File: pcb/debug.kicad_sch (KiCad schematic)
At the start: 8 parts

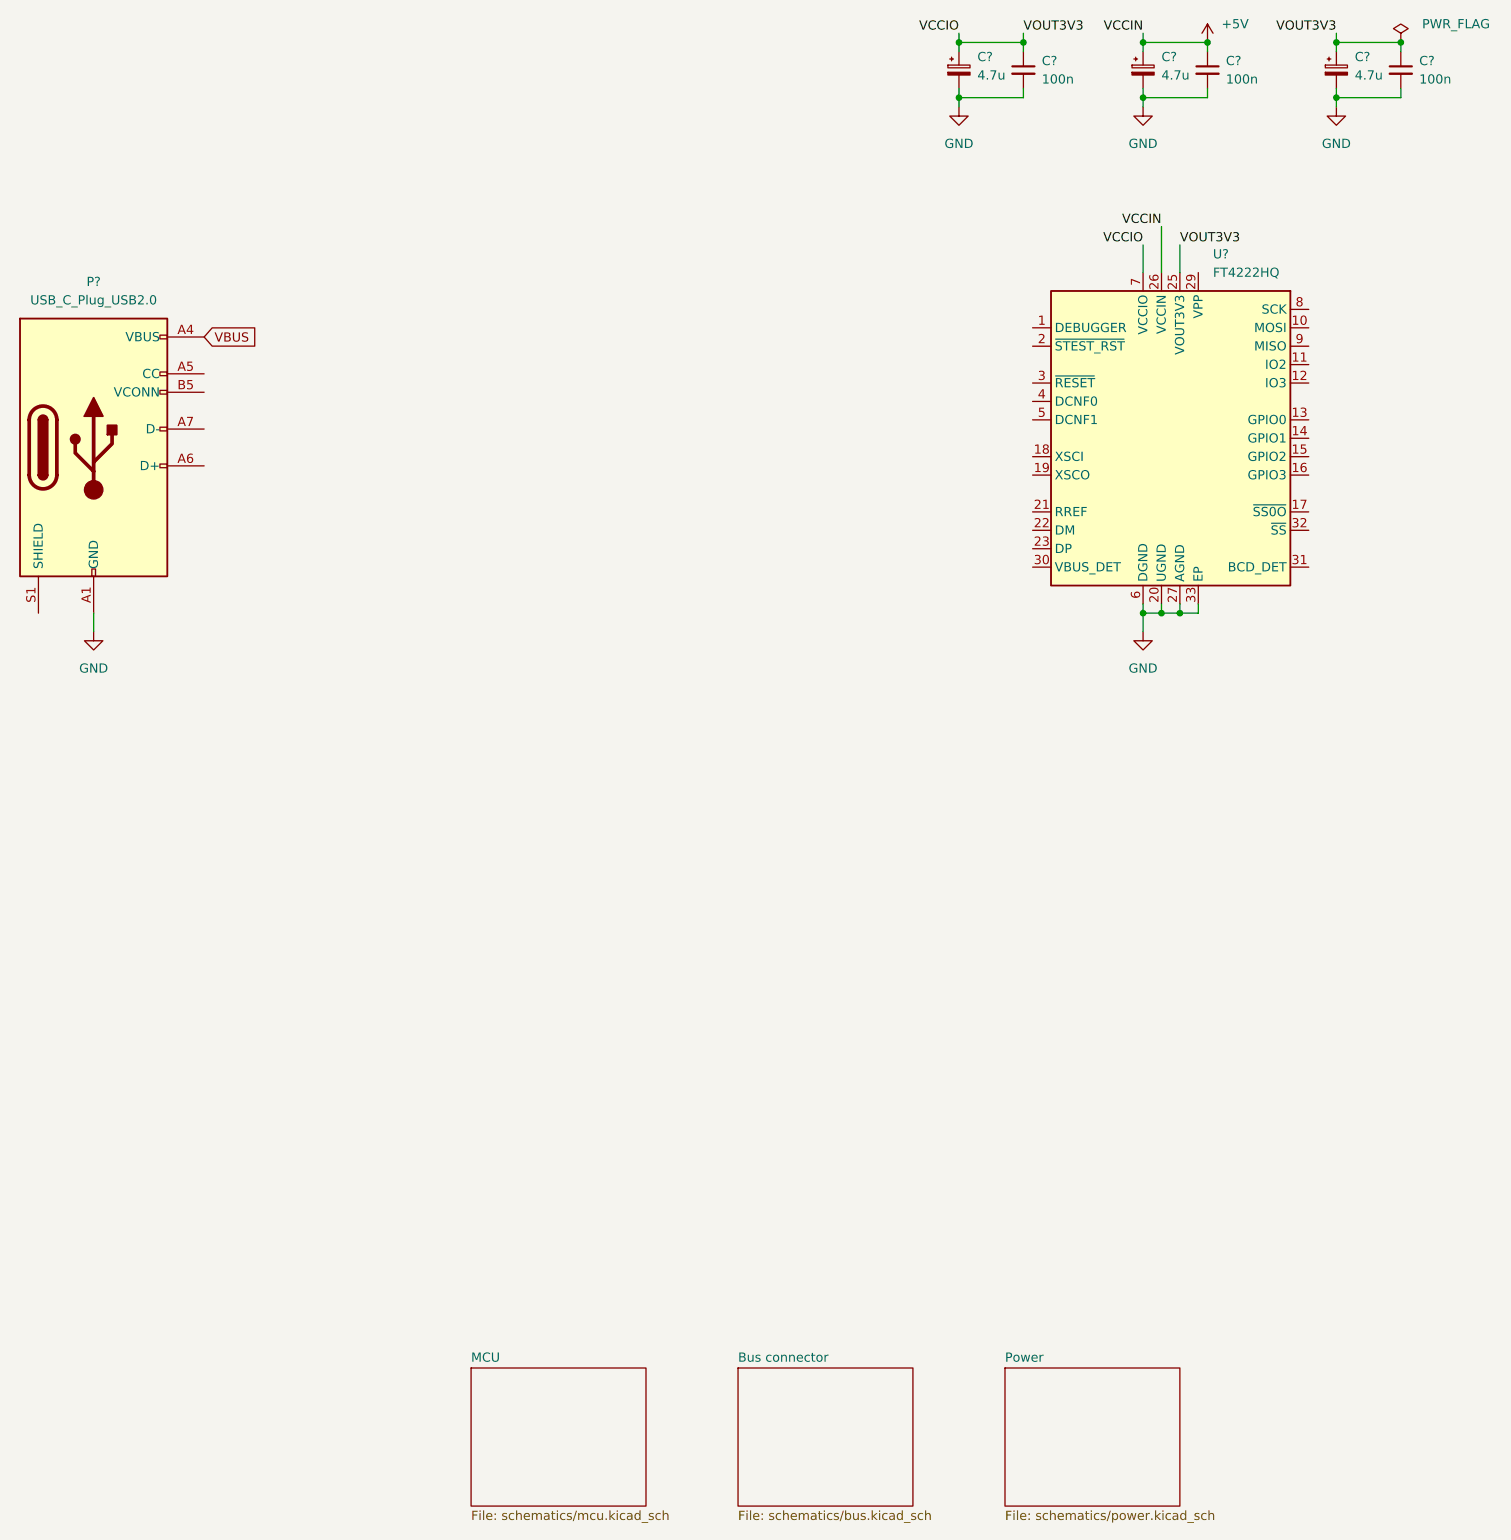
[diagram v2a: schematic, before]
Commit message: start choosing components, need to add overcurren t protection
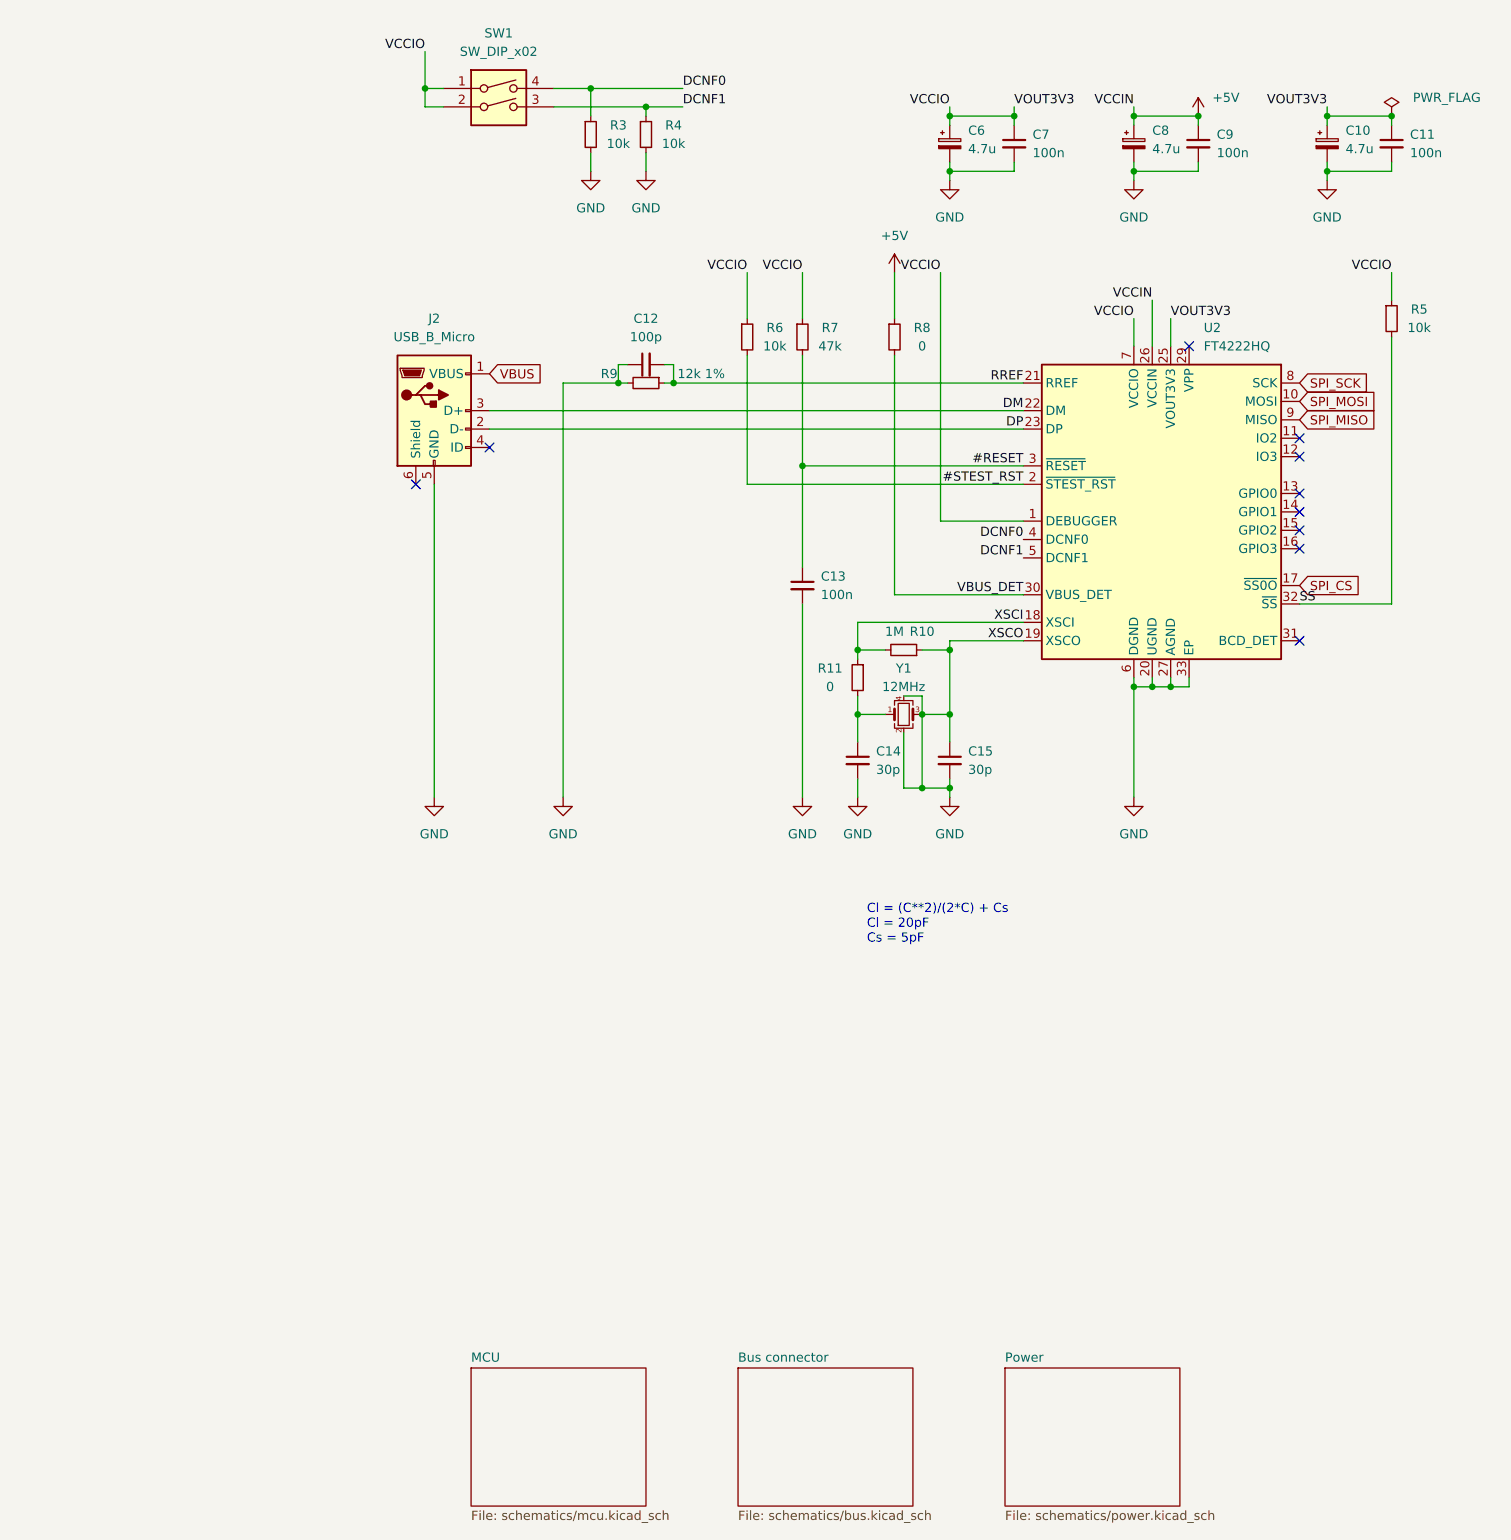
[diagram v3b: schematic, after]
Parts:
- removed P?: USB_C_Plug_USB2.0, symbol Connector:USB_C_Plug_USB2.0
- added C12: 100p, Capacitor_SMD:C_0603_1608Metric, symbol Device:C_Small
- added C13: 100n, Capacitor_SMD:C_0603_1608Metric, symbol Device:C_Small
- added C14, C15: 30p, Capacitor_SMD:C_0603_1608Metric, symbol Device:C_Small
- added J2: USB_B_Micro, symbol Connector:USB_B_Micro
- added R10: 1M, symbol Device:R_Small
- added R11, R8: 0, symbol Device:R_Small
- added R3, R4, R5, R6: 10k, symbol Device:R_Small
- added R7: 47k, symbol Device:R_Small
- added R9: 12k 1%, symbol Device:R_Small
- added SW1: SW_DIP_x02, symbol Switch:SW_DIP_x02
- added Y1: 12MHz, ECS-120-18-33-JGN-TR:XTAL_ECS-120-18-33-JGN-TR, symbol Device:Crystal_GND24_Small
- C10, C6, C8: renamed from C?; footprint (none) -> Capacitor_SMD:C_0805_2012Metric; Part Number (none) -> GRM21BR71C475KE51L
- C11, C7, C9: renamed from C?; footprint (none) -> Capacitor_SMD:C_0603_1608Metric; Part Number (none) -> 885012206095
- U2: renamed from U?; Part Number (none) -> FT4222HQ-D-R
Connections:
- net +5V: now also R8.1
- net GND: now also U2.19 (XSCO), C12.1, C13.2, C14.2, C15.1, C15.2, J2.5 (GND), R10.1, R3.2, R4.2, R9.2, Y1.2, Y1.3, Y1.4
- net VBUS: now also J2.1 (VBUS)
- net VCCIO: now also U2.1 (DEBUGGER), R5.1, R6.1, R7.1, SW1.1, SW1.2
- net SPI_MOSI: now reaches U2.10 (MOSI)
- net SPI_CS: now reaches U2.17 (~{SS0O})
- net XSCI: now reaches U2.18 (XSCI)
- net XSCI: now also R10.2, R11.1
- net #STEST_RST: now reaches U2.2 (~{STEST_RST})
- net #STEST_RST: now also R6.2
- net RREF: now reaches U2.21 (RREF)
- net RREF: now also C12.2, R9.1
- net DM: now reaches U2.22 (DM)
- net DM: now also J2.3 (D+)
- net DP: now reaches U2.23 (DP)
- net DP: now also J2.2 (D-)
- net #RESET: now reaches U2.3 (~{RESET})
- net #RESET: now also C13.1, R7.2
- net VBUS_DET: now reaches U2.30 (VBUS_DET)
- net VBUS_DET: now also R8.2
- net SS: now reaches U2.32 (~{SS})
- net SS: now also R5.2
- net DCNF0: now reaches U2.4 (DCNF0)
- net DCNF0: now also R3.1, SW1.4
- net DCNF1: now reaches U2.5 (DCNF1)
- net DCNF1: now also R4.1, SW1.3
- net SPI_SCK: now reaches U2.8 (SCK)
- net SPI_MISO: now reaches U2.9 (MISO)
- new net: C14.1, R11.2, Y1.1
- no-connect marks 0 -> 10
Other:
- note added: "Cl = (C**2)/(2*C) + Cs Cl = 20pF Cs = 5pF"
- moved on the sheet: C10, C11, C6, C7, C8, C9, U2

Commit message: finish the schematic
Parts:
- J2: footprint (none) -> 10118194-0001LF:AMPHENOL_10118194-0001LF; Part Number (none) -> 10118194-0001LF
- R10: footprint (none) -> Resistor_SMD:R_0603_1608Metric; Part Number (none) -> CR0603-FX-1004ELF
- R11, R8: footprint (none) -> Resistor_SMD:R_0603_1608Metric; Part Number (none) -> CR0603-J/-000ELF
- R3, R4, R5, R6: footprint (none) -> Resistor_SMD:R_0603_1608Metric; Part Number (none) -> CR0603-FX-1002ELF
- R7: footprint (none) -> Resistor_SMD:R_0603_1608Metric; Part Number (none) -> AC0603FR-0747KL
- R9: footprint (none) -> Resistor_SMD:R_0603_1608Metric; Part Number (none) -> RC0603FR-1012KL
- SW1: footprint (none) -> DS04-254-2-02BK-SMT:SW_DS04-254-2-02BK-SMT; Part Number (none) -> DS04-254-2-02BK-SMT
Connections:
- net GND: no longer C15.1, R10.1, U2.19 (XSCO), Y1.3
- new net XSCO: C15.1, R10.1, U2.19 (XSCO), Y1.3

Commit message: add components to the pcb
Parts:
- removed J2: USB_B_Micro, 10118194-0001LF:AMPHENOL_10118194-0001LF, symbol Connector:USB_B_Micro
- added J2: USB_C_Receptacle_USB2.0, USB4105-GF-A:GCT_USB4105-GF-A, symbol Connector:USB_C_Receptacle_USB2.0
- added R18, R19: 5.1k, Resistor_SMD:R_0603_1608Metric, symbol Device:R_Small
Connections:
- net DM: now also J2.A7 (D-), J2.B7 (D-)
- net DP: now also J2.A6 (D+), J2.B6 (D+)
- net GND: now also J2.A1 (GND), J2.A12 (GND), J2.B1 (GND), J2.B12 (GND), R18.2, R19.2
- net VBUS: now also J2.A4 (VBUS), J2.A9 (VBUS), J2.B4 (VBUS), J2.B9 (VBUS)
- new net: J2.A5 (CC1), R19.1
- new net: J2.B5 (CC2), R18.1
- no-connect marks 10 -> 11

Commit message: finished placing components
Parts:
- added H1, H2, H3, H4: MountingHole, MountingHole:MountingHole_2.7mm_M2.5, symbol Mechanical:MountingHole
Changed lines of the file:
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@@
     (pin "1")
+  )
+  (symbol (lib_id "Mechanical:MountingHole") (at 38.1 226.06 0) (unit 1)
+    (in_bom yes) (on_board yes) (fields_autoplaced)
+    (property "Reference" "H1" (id 0) (at 40.64 224.7899 0)
+      (effects (font (size 1.27 1.27)) (justify left))
+    )
+    (property "Value" "MountingHole" (id 1) (at 40.64 227.3299 0)
+      (effects (font (size 1.27 1.27)) (justify left))
+    )
+    (property "Footprint" "MountingHole:MountingHole_2.7mm_M2.5" (id 2) (at 38.1 226.06 0)
+      (effects (font (size 1.27 1.27)) hide)
+    )
+    (property "Datasheet" "~" (id 3) (at 38.1 226.06 0)
+      (effects (font (size 1.27 1.27)) hide)
+    )
   )
   (symbol (lib_id "power:GND") (at 189.23 140.97 0) (unit 1)
@@
     )
     (pin "1")
+  )
+  (symbol (lib_id "Mechanical:MountingHole") (at 57.15 226.06 0) (unit 1)
+    (in_bom yes) (on_board yes) (fields_autoplaced)
+    (property "Reference" "H2" (id 0) (at 59.69 224.7899 0)
+      (effects (font (size 1.27 1.27)) (justify left))
+    )
+    (property "Value" "MountingHole" (id 1) (at 59.69 227.3299 0)
+      (effects (font (size 1.27 1.27)) (justify left))
+    )
+    (property "Footprint" "MountingHole:MountingHole_2.7mm_M2.5" (id 2) (at 57.15 226.06 0)
+      (effects (font (size 1.27 1.27)) hide)
+    )
+    (property "Datasheet" "~" (id 3) (at 57.15 226.06 0)
+      (effects (font (size 1.27 1.27)) hide)
+    )
+  )
+  (symbol (lib_id "Mechanical:MountingHole") (at 57.15 231.14 0) (unit 1)
+    (in_bom yes) (on_board yes) (fields_autoplaced)
+    (property "Reference" "H4" (id 0) (at 59.69 229.8699 0)
+      (effects (font (size 1.27 1.27)) (justify left))
+    )
+    (property "Value" "MountingHole" (id 1) (at 59.69 232.4099 0)
+      (effects (font (size 1.27 1.27)) (justify left))
+    )
+    (property "Footprint" "MountingHole:MountingHole_2.7mm_M2.5" (id 2) (at 57.15 231.14 0)
+      (effects (font (size 1.27 1.27)) hide)
+    )
+    (property "Datasheet" "~" (id 3) (at 57.15 231.14 0)
+      (effects (font (size 1.27 1.27)) hide)
+    )
   )
   (symbol (lib_id "Device:C_Polarized_Small") (at 215.9 50.8 0) (unit 1)
@@
     (pin "1")
   )
+  (symbol (lib_id "Mechanical:MountingHole") (at 38.1 231.14 0) (unit 1)
+    (in_bom yes) (on_board yes) (fields_autoplaced)
+    (property "Reference" "H3" (id 0) (at 40.64 229.8699 0)
+      (effects (font (size 1.27 1.27)) (justify left))
+    )
+    (property "Value" "MountingHole" (id 1) (at 40.64 232.4099 0)
+      (effects (font (size 1.27 1.27)) (justify left))
+    )
+    (property "Footprint" "MountingHole:MountingHole_2.7mm_M2.5" (id 2) (at 38.1 231.14 0)
+      (effects (font (size 1.27 1.27)) hide)
+    )
+    (property "Datasheet" "~" (id 3) (at 38.1 231.14 0)
+      (effects (font (size 1.27 1.27)) hide)
+    )
+  )
   (symbol (lib_id "power:GND") (at 104.14 140.97 0) (unit 1)
     (in_bom yes) (on_board yes) (fields_autoplaced)
@@
       (reference "FB2") (unit 1) (value "100") (footprint "Inductor_SMD:L_0805_2012Metric")
     )
+    (path "/50bf00c7-c69d-47e9-8d7f-002d8001f5dd"
+      (reference "H1") (unit 1) (value "MountingHole") (footprint "MountingHole:MountingHole_2.7mm_M2.5")
+    )
+    (path "/6b396c70-f728-455a-acfe-72630436df78"
+      (reference "H2") (unit 1) (value "MountingHole") (footprint "MountingHole:MountingHole_2.7mm_M2.5")
+    )
+    (path "/e5ddd04d-76f1-4f42-ab4b-980719c3dba6"
+      (reference "H3") (unit 1) (value "MountingHole") (footprint "MountingHole:MountingHole_2.7mm_M2.5")
+    )
+    (path "/76e69ec1-8d90-4427-bc70-b576047b6213"
+      (reference "H4") (unit 1) (value "MountingHole") (footprint "MountingHole:MountingHole_2.7mm_M2.5")
+    )
     (path "/dfea10a7-1cbe-4c44-a951-08c8c82414b9/4ec00cc8-73ee-4a88-8f61-16dd24bb6fe7"
